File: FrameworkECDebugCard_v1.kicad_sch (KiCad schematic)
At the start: 29 parts, among them J1 Conn_01x05, P1 1054440011, P2 2169900001, U1 FT230XS

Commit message: ec3: route it! use JLCPCB's tolerances
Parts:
- TP1, TP2, TP3, TP4: footprint TestPoint:TestPoint_Pad_1.5x1.5mm -> TestPoint:TestPoint_Pad_1.0x1.0mm
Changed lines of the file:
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@@
 			)
 		)
-		(property "Footprint" "TestPoint:TestPoint_Pad_1.5x1.5mm"
+		(property "Footprint" "TestPoint:TestPoint_Pad_1.0x1.0mm"
 			(at 255.27 22.86 0)
 			(effects
@@
 			)
 		)
-		(property "Footprint" "TestPoint:TestPoint_Pad_1.5x1.5mm"
+		(property "Footprint" "TestPoint:TestPoint_Pad_1.0x1.0mm"
 			(at 243.84 22.86 0)
 			(effects
@@
 			)
 		)
-		(property "Footprint" "TestPoint:TestPoint_Pad_1.5x1.5mm"
+		(property "Footprint" "TestPoint:TestPoint_Pad_1.0x1.0mm"
 			(at 243.84 29.21 0)
 			(effects
@@
 			)
 		)
-		(property "Footprint" "TestPoint:TestPoint_Pad_1.5x1.5mm"
+		(property "Footprint" "TestPoint:TestPoint_Pad_1.0x1.0mm"
 			(at 255.27 29.21 0)
 			(effects

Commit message: ec3: switch to 'real' molex footprint
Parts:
- P2: footprint FrameworkECDebugCard_v1:USB4510-03-1-A_GCT -> FrameworkECDebugCard_v1:MOLEX_2169900001
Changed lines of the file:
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@@
 			)
 		)
-		(property "Footprint" "FrameworkECDebugCard_v1:USB4510-03-1-A_GCT"
+		(property "Footprint" "FrameworkECDebugCard_v1:MOLEX_2169900001"
 			(at 27.94 38.1 0)
 			(effects

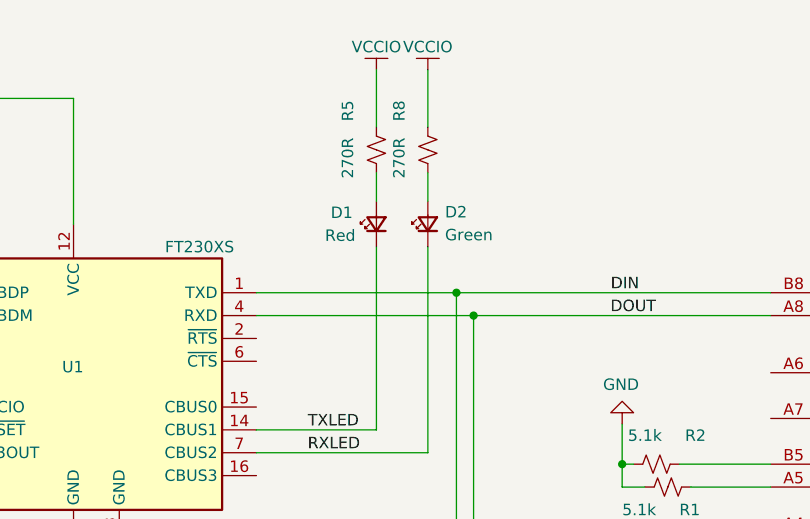
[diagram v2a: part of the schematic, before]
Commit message: ec3: specify LEDs, some pad types
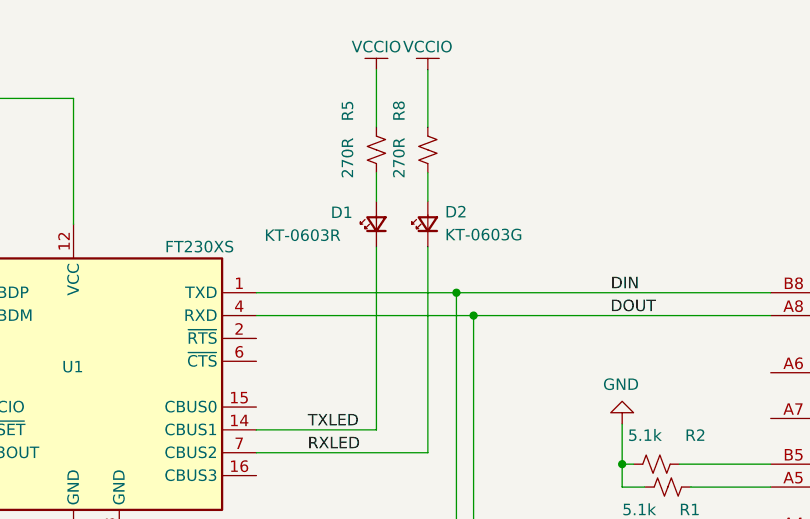
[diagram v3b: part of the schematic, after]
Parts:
- D1: value Red -> KT-0603R
- D2: value Green -> KT-0603G
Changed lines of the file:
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@@
 			)
 		)
-		(property "Value" "Red"
-			(at 111.125 38.1 90)
+		(property "Value" "KT-0603R"
+			(at 104.394 38.1 90)
 			(effects
 				(font
@@
 			)
 		)
-		(property "Value" "Green"
+		(property "Value" "KT-0603G"
 			(at 124.46 38.0364 90)
 			(effects

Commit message: ec3: geographical reannotate
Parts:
- renumbered C2 to C1, C3 to C2, C4 to C3, C1 to C4, H3 to H2, H2 to H3, R5 to R4, R4 to R5
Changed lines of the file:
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@@
 		(on_board yes)
 		(dnp yes)
-		(property "Reference" "H2"
+		(property "Reference" "H3"
 			(at 265.43 27.9654 0)
 			(effects
@@
 			(project ""
 				(path "/6d9454a9-630b-4948-a74b-a7b030d302e8"
-					(reference "H2")
+					(reference "H3")
 					(unit 1)
 				)
@@
 		(on_board yes)
 		(dnp yes)
-		(property "Reference" "H3"
+		(property "Reference" "H2"
 			(at 265.43 40.6654 0)
 			(effects
@@
 			(project "FrameworkECDebugCard_v1"
 				(path "/6d9454a9-630b-4948-a74b-a7b030d302e8"
-					(reference "H3")
+					(reference "H2")
 					(unit 1)
 				)
@@
 		(dnp no)
 		(fields_autoplaced yes)
-		(property "Reference" "C4"
+		(property "Reference" "C3"
 			(at 31.75 109.8549 0)
 			(effects
@@
 			(project ""
 				(path "/6d9454a9-630b-4948-a74b-a7b030d302e8"
-					(reference "C4")
+					(reference "C3")
 					(unit 1)
 				)
@@
 		(on_board yes)
 		(dnp no)
-		(property "Reference" "R4"
+		(property "Reference" "R5"
 			(at 58.42 41.275 90)
 			(effects
@@
 			(project ""
 				(path "/6d9454a9-630b-4948-a74b-a7b030d302e8"
-					(reference "R4")
+					(reference "R5")
 					(unit 1)
 				)
@@
 		(dnp no)
 		(fields_autoplaced yes)
-		(property "Reference" "C3"
+		(property "Reference" "C2"
 			(at 45.72 109.8549 0)
 			(effects
@@
 			(project ""
 				(path "/6d9454a9-630b-4948-a74b-a7b030d302e8"
-					(reference "C3")
+					(reference "C2")
 					(unit 1)
 				)
@@
 		(on_board yes)
 		(dnp no)
-		(property "Reference" "R5"
+		(property "Reference" "R4"
 			(at 113.665 25.4 90)
 			(effects
@@
 			(project ""
 				(path "/6d9454a9-630b-4948-a74b-a7b030d302e8"
-					(reference "R5")
+					(reference "R4")
 					(unit 1)
 				)
@@
 		(dnp no)
 		(fields_autoplaced yes)
-		(property "Reference" "C2"
+		(property "Reference" "C1"
 			(at 62.865 78.1049 0)
 			(effects
@@
 			(project ""
 				(path "/6d9454a9-630b-4948-a74b-a7b030d302e8"
-					(reference "C2")
+					(reference "C1")
 					(unit 1)
 				)
@@
 		(on_board yes)
 		(dnp no)
-		(property "Reference" "C1"
+		(property "Reference" "C4"
 			(at 29.21 67.31 0)
 			(effects
@@
 			(project ""
 				(path "/6d9454a9-630b-4948-a74b-a7b030d302e8"
-					(reference "C1")
-					(unit 1)
-				)
+					(reference "C4")
+					(unit 1)
+				)

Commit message: Upgrade to KiCad 9
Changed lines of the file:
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@@
 (kicad_sch
-	(version 20231120)
+	(version 20250114)
 	(generator "eeschema")
-	(generator_version "8.0")
+	(generator_version "9.0")
 	(paper "A4")
 	(title_block
@@
 		(comment 4 "https://howett.net")
 	)
+	(text "Mechanical mounting"
+		(exclude_from_sim no)
+		(at 237.49 36.83 0)
+		(effects
+			(font
+				(size 2.54 2.54)
+			)
+			(justify left bottom)
+		)
+	)
+	(text "USB-C Plug"
+		(exclude_from_sim no)
+		(at 187.325 82.55 0)
+		(effects
+			(font
+				(size 2.54 2.54)
+			)
+			(justify right bottom)
+		)
+	)
 	(junction
 		(at 39.37 41.91)
@@
 		)
 	)
-	(text "Mechanical mounting"
-		(exclude_from_sim no)
-		(at 237.49 36.83 0)
-		(effects
-			(font
-				(size 2.54 2.54)
-			)
-			(justify left bottom)
-		)
-	)
-	(text "USB-C Plug"
-		(exclude_from_sim no)
-		(at 187.325 82.55 0)
-		(effects
-			(font
-				(size 2.54 2.54)
-			)
-			(justify right bottom)
-		)
-	)
 	(label "F_USBD-"
 		(at 60.96 46.99 0)
-		(fields_autoplaced yes)
 		(effects
 			(font
@@
 	(label "DIN"
 		(at 142.875 44.45 0)
-		(fields_autoplaced yes)
 		(effects
 			(font
@@
 	(label "TXLED"
 		(at 109.22 59.69 0)
-		(fields_autoplaced yes)
 		(effects
 			(font
@@
 	(label "F_USBD+"
 		(at 60.96 44.45 0)
-		(fields_autoplaced yes)
 		(effects
 			(font
@@
 	(label "USBD-"
 		(at 50.165 50.9111 0)
-		(fields_autoplaced yes)
 		(effects
 			(font
@@
 	(label "RXLED"
 		(at 109.2021 62.23 0)
-		(fields_autoplaced yes)
 		(effects
 			(font
@@
 	(label "DOUT"
 		(at 142.8412 46.99 0)
-		(fields_autoplaced yes)
 		(effects
 			(font
@@
 	(label "USBD+"
 		(at 44.45 44.45 0)
-		(fields_autoplaced yes)
 		(effects
 			(font
@@
 		)
 	)
+	(embedded_fonts no)
 )

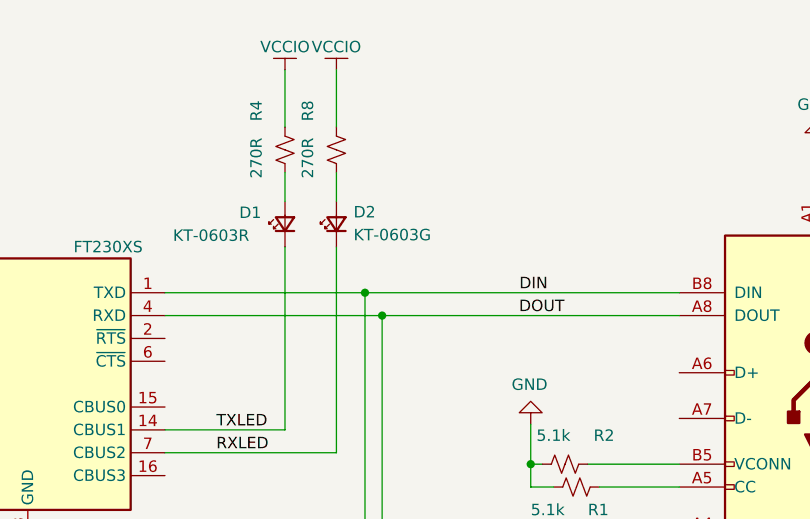
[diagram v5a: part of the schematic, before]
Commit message: Add JLCPCB LCSC part numbers
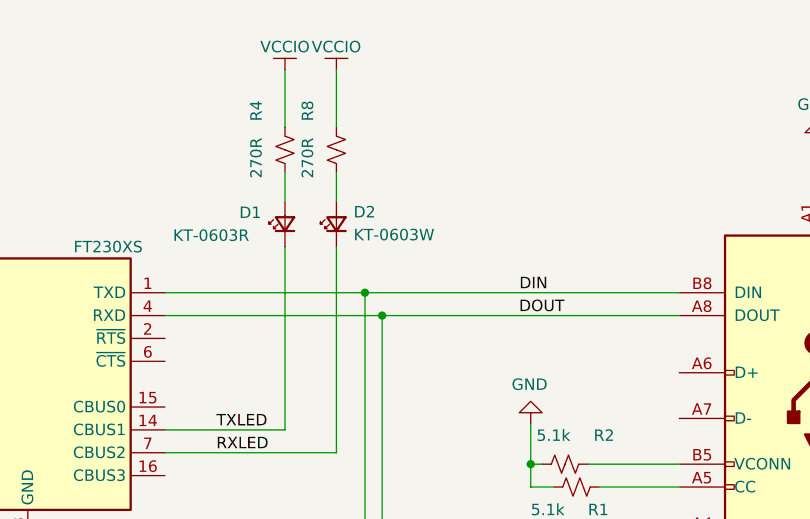
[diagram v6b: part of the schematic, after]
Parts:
- C1, C3: LCSC (none) -> C307331
- C2: LCSC (none) -> C23733
- C4: LCSC (none) -> C15195
- C5, C6: LCSC (none) -> C1567
- D1: LCSC (none) -> C2286
- D2: value KT-0603G -> KT-0603W; LCSC (none) -> C2290
- FB1: LCSC (none) -> C76886
- H1, H2, H3, H4, TP1, TP2, TP3, TP4: now left out of the parts list
- P1: LCSC (none) -> C561769
- P2: LCSC (none) -> C2843969
- R1, R2, R3, R6: LCSC (none) -> C25905
- R4, R8: LCSC (none) -> C25099
- R5, R7: LCSC (none) -> C25100
- U1: LCSC (none) -> C69082
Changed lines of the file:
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@@
+			)
+		)
+		(property "LCSC" "C561769"
+			(at 175.895 55.88 0)
+			(effects
+				(font
+					(size 1.27 1.27)
+				)
+				(hide yes)
 			)
 		)
@@
 			)
 		)
+		(property "LCSC" "C25905"
+			(at 149.225 66.04 90)
+			(effects
+				(font
+					(size 1.27 1.27)
+				)
+				(hide yes)
+			)
+		)
 		(pin "1"
 		)
@@
 		(unit 1)
 		(exclude_from_sim no)
-		(in_bom yes)
+		(in_bom no)
 		(on_board yes)
 		(dnp yes)
@@
 		(unit 1)
 		(exclude_from_sim no)
-		(in_bom yes)
+		(in_bom no)
 		(on_board yes)
 		(dnp yes)
@@
 		(unit 1)
 		(exclude_from_sim no)
-		(in_bom yes)
+		(in_bom no)
 		(on_board yes)
 		(dnp yes)
@@
 		(unit 1)
 		(exclude_from_sim no)
-		(in_bom yes)
+		(in_bom no)
 		(on_board yes)
 		(dnp yes)
@@
 		(unit 1)
 		(exclude_from_sim no)
-		(in_bom yes)
+		(in_bom no)
 		(on_board yes)
 		(dnp yes)
@@
 		(unit 1)
 		(exclude_from_sim no)
-		(in_bom yes)
+		(in_bom no)
 		(on_board yes)
 		(dnp yes)
@@
 		(unit 1)
 		(exclude_from_sim no)
-		(in_bom yes)
+		(in_bom no)
 		(on_board yes)
 		(dnp yes)
@@
 			)
 		)
+		(property "LCSC" "C2286"
+			(at 116.84 36.83 90)
+			(effects
+				(font
+					(size 1.27 1.27)
+				)
+				(hide yes)
+			)
+		)
 		(pin "1"
 		)
@@
 		)
 		(property "Description" ""
+			(at 44.45 59.055 0)
+			(effects
+				(font
+					(size 1.27 1.27)
+				)
+				(hide yes)
+			)
+		)
+		(property "LCSC" "C1567"
 			(at 44.45 59.055 0)
 			(effects
@@
 			)
 		)
+		(property "LCSC" "C25100"
+			(at 52.07 44.45 90)
+			(effects
+				(font
+					(size 1.27 1.27)
+				)
+				(hide yes)
+			)
+		)
 		(pin "1"
 		)
@@
 		(property "Description" ""
 			(at 147.955 63.5 0)
+			(effects
+				(font
+					(size 1.27 1.27)
+				)
+				(hide yes)
+			)
+		)
+		(property "LCSC" "C25905"
+			(at 147.955 63.5 90)
 			(effects
 				(font
@@
 			)
 		)
+		(property "LCSC" "C1567"
+			(at 50.165 59.055 0)
+			(effects
+				(font
+					(size 1.27 1.27)
+				)
+				(hide yes)
+			)
+		)
 		(pin "1"
 		)
@@
 			)
 		)
+		(property "LCSC" "C307331"
+			(at 27.94 111.125 0)
+			(effects
+				(font
+					(size 1.27 1.27)
+				)
+				(hide yes)
+			)
+		)
 		(pin "1"
 		)
@@
 			)
 		)
+		(property "LCSC" "C25100"
+			(at 58.42 46.99 90)
+			(effects
+				(font
+					(size 1.27 1.27)
+				)
+				(hide yes)
+			)
+		)
 		(pin "1"
 		)
@@
 		(property "Description" ""
 			(at 46.99 22.86 0)
+			(effects
+				(font
+					(size 1.27 1.27)
+				)
+				(hide yes)
+			)
+		)
+		(property "LCSC" "C76886"
+			(at 46.99 22.86 90)
 			(effects
 				(font
@@
 			)
 		)
-		(property "Value" "KT-0603G"
+		(property "Value" "KT-0603W"
 			(at 124.46 38.0364 90)
 			(effects
@@
 			)
 		)
+		(property "LCSC" "C2290"
+			(at 122.555 36.83 90)
+			(effects
+				(font
+					(size 1.27 1.27)
+				)
+				(hide yes)
+			)
+		)
 		(pin "1"
 		)
@@
 		(property "Description" "Resistor, small US symbol"
 			(at 45.72 30.48 0)
+			(effects
+				(font
+					(size 1.27 1.27)
+				)
+				(hide yes)
+			)
+		)
+		(property "LCSC" "C25905"
+			(at 45.72 30.48 90)
 			(effects
 				(font
@@
 			)
 		)
+		(property "LCSC" "C2843969"
+			(at 24.13 38.1 0)
+			(effects
+				(font
+					(size 1.27 1.27)
+				)
+				(hide yes)
+			)
+		)
 		(pin "B9"
 		)
@@
 			)
 		)
+		(property "LCSC" "C23733"
+			(at 41.91 111.125 0)
+			(effects
+				(font
+					(size 1.27 1.27)
+				)
+				(hide yes)
+			)
+		)
 		(pin "1"
 		)
@@
 			)
 		)
+		(property "LCSC" "C25905"
+			(at 45.72 27.94 90)
+			(effects
+				(font
+					(size 1.27 1.27)
+				)
+				(hide yes)
+			)
+		)
 		(pin "2"
 		)
@@
 			)
 		)
+		(property "LCSC" "C25099"
+			(at 116.84 28.575 90)
+			(effects
+				(font
+					(size 1.27 1.27)
+				)
+				(hide yes)
+			)
+		)
 		(pin "1"
 		)
@@
 		)
 		(property "Description" ""
+			(at 85.725 54.61 0)
+			(effects
+				(font
+					(size 1.27 1.27)
+				)
+				(hide yes)
+			)
+		)
+		(property "LCSC" "C69082"
 			(at 85.725 54.61 0)
 			(effects
@@
 			)
 		)
+		(property "LCSC" "C307331"
+			(at 59.055 79.375 0)
+			(effects
+				(font
+					(size 1.27 1.27)
+				)
+				(hide yes)
+			)
+		)
 		(pin "1"
 		)
@@
 			)
 		)
+		(property "LCSC" "C15195"
+			(at 34.29 66.04 0)
+			(effects
+				(font
+					(size 1.27 1.27)
+				)
+				(hide yes)
+			)
+		)
 		(pin "1"
 		)
@@
 		(unit 1)
 		(exclude_from_sim no)
-		(in_bom yes)
+		(in_bom no)
 		(on_board yes)
 		(dnp yes)
@@
 			(effects
 				(font
+					(size 1.27 1.27)
+				)
+				(hide yes)
+			)
+		)
+		(property "LCSC" "C25099"
+			(at 122.555 28.575 90)
+			(effects
+				(font

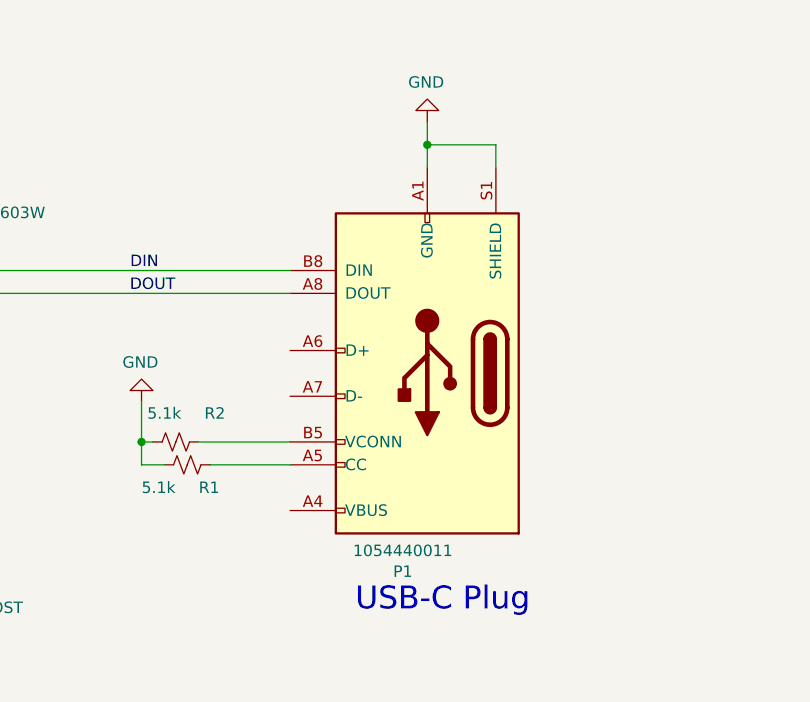
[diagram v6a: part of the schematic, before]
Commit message: Fabrication files export settings (PCBWay etc)
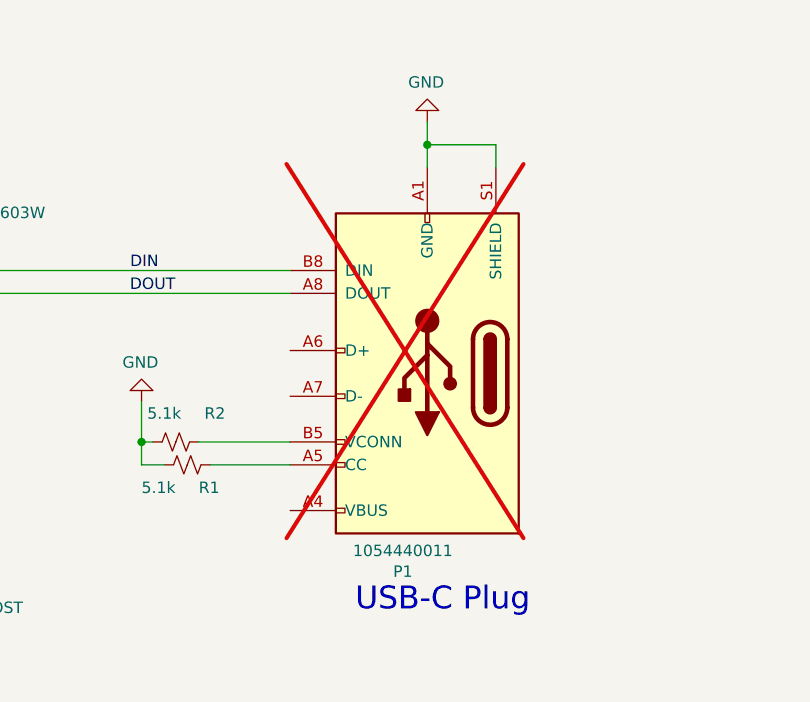
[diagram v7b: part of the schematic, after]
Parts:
- P1: now not fitted
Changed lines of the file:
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@@
 		(in_bom yes)
 		(on_board yes)
-		(dnp no)
+		(dnp yes)
 		(property "Reference" "P1"
 			(at 173.1772 77.9018 0)
